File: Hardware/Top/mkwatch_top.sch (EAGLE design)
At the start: 64 parts, among them SW5 SWITCH.MOM, SW6 SWITCH.MOM, U1 NRF52832_MODULE_MDBT42, U4 FT231XS, U5 PCF8523

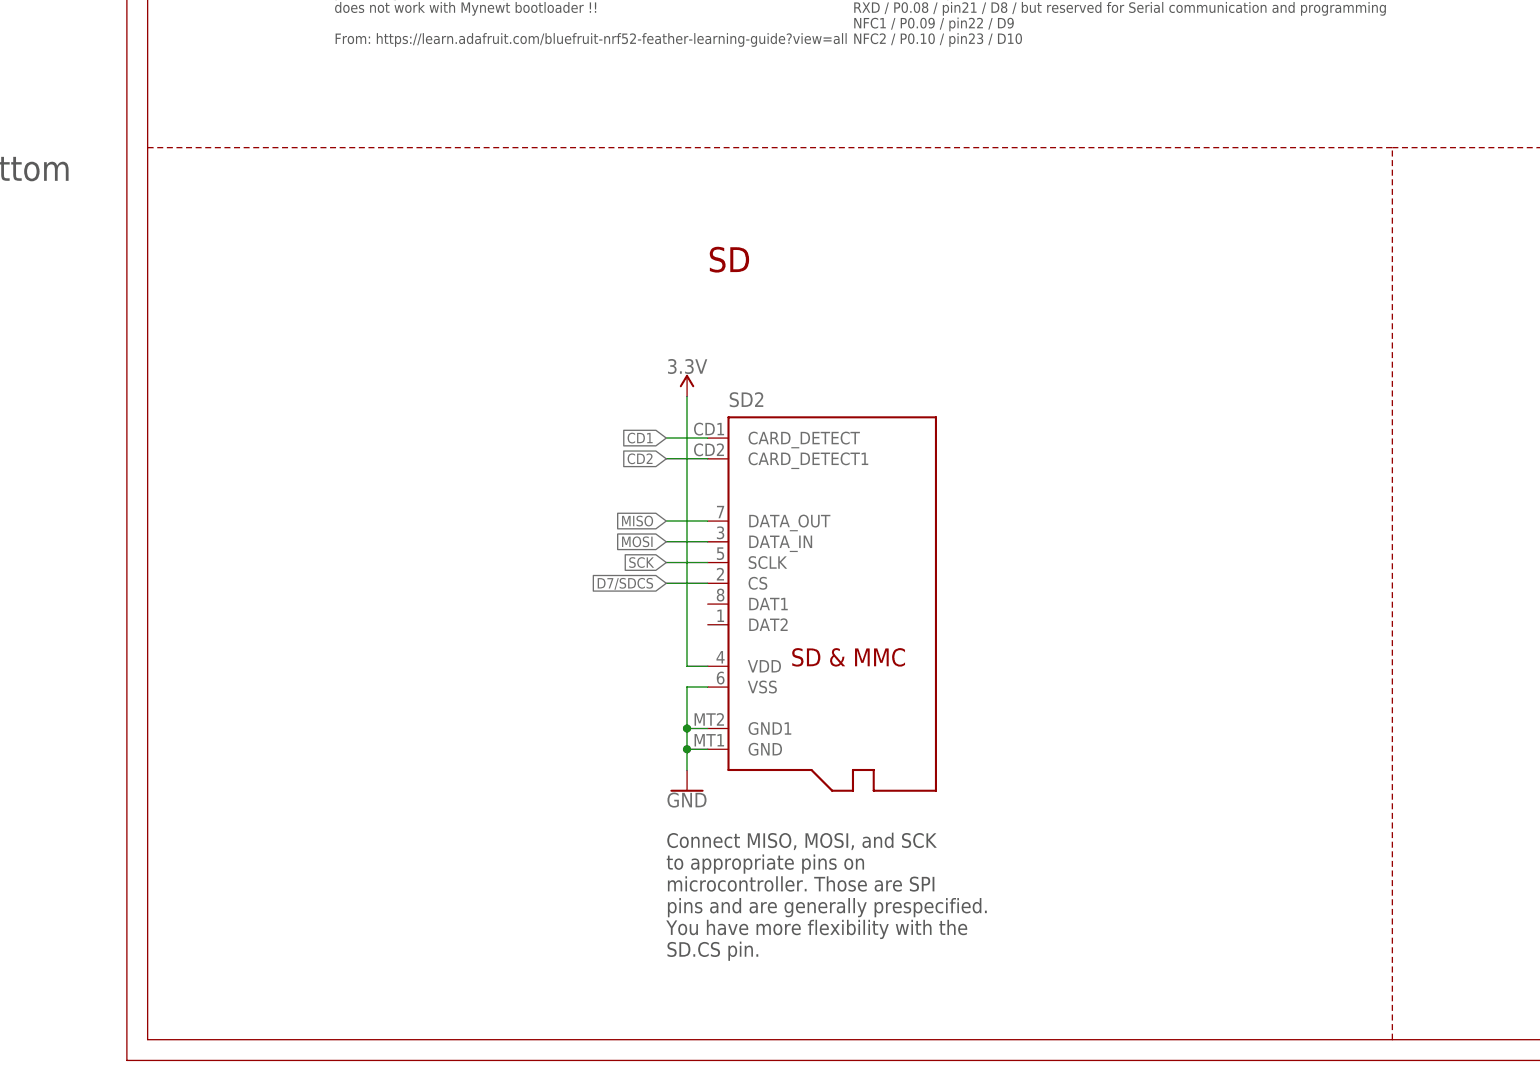
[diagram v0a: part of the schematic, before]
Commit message: added 7pin connector to schematic and board for comm between top and bottom board
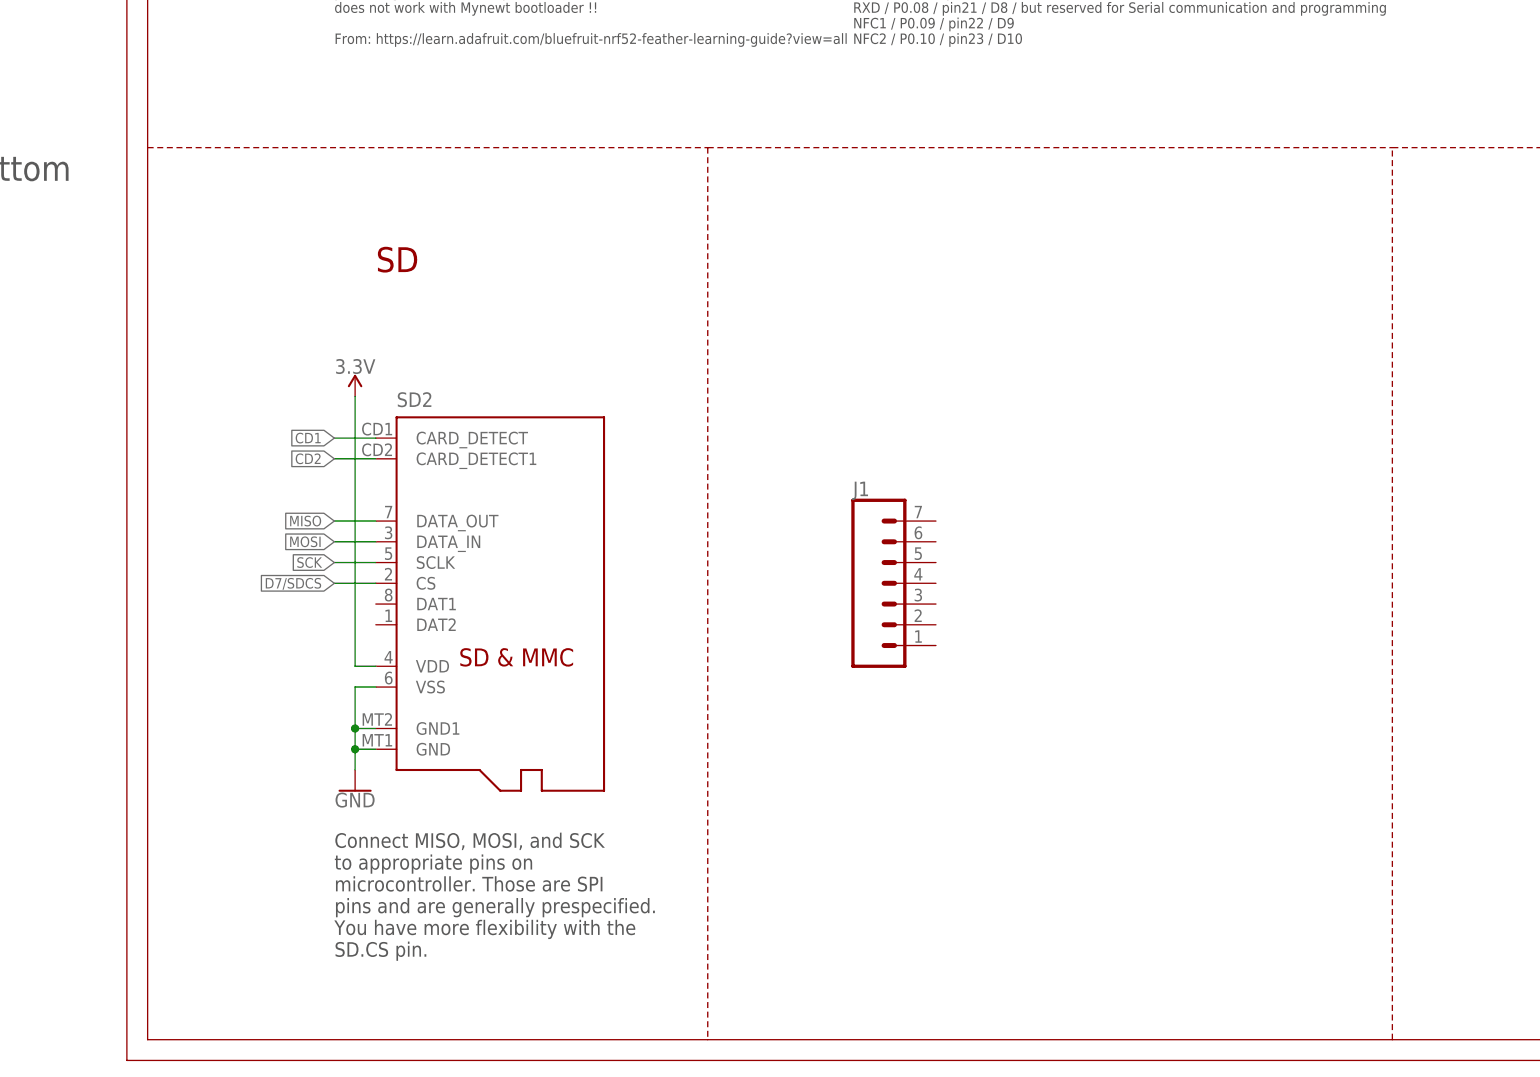
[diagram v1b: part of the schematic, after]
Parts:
- added J1: (no value), LinnesLab-Connectors:CONN_07-1.27MM
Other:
- moved on the sheet: SD2
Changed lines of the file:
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@@
 <part name="R9" library="LinnesLab-Passives" deviceset="RESISTOR" device="0402" package3d_urn="urn:adsk.eagle:package:15661898/2" value="10k"/>
 <part name="SUPPLY3" library="LinnesLab-Symbols" deviceset="3.3V" device=""/>
+<part name="J1" library="LinnesLab-Connectors" deviceset="CONN_07" device="-1.27MM"/>
 </parts>
 <sheets>
@@
 <text x="-83.82" y="-30.48" size="3.048" layer="94">Power Man.</text>
 <text x="73.66" y="-73.66" size="3.048" layer="94">Buttons</text>
-<text x="-238.76" y="-22.86" size="3.048" layer="94">SD</text>
+<text x="-279.4" y="-22.86" size="3.048" layer="94">SD</text>
 <text x="119.38" y="-48.26" size="1.27" layer="97">I2C Address = 0x68h</text>
 <text x="73.66" y="-50.8" size="1.27" layer="97">Back-up
@@
 <wire x1="-307.34" y1="162.56" x2="-307.34" y2="-7.62" width="0.1524" layer="94"/>
 <wire x1="-307.34" y1="-7.62" x2="-307.34" y2="-116.84" width="0.1524" layer="94"/>
-<wire x1="-307.34" y1="-116.84" x2="-154.94" y2="-116.84" width="0.1524" layer="94"/>
+<wire x1="-307.34" y1="-116.84" x2="-238.76" y2="-116.84" width="0.1524" layer="94"/>
+<wire x1="-238.76" y1="-116.84" x2="-154.94" y2="-116.84" width="0.1524" layer="94"/>
 <wire x1="-154.94" y1="-116.84" x2="15.24" y2="-116.84" width="0.1524" layer="94"/>
 <wire x1="15.24" y1="-116.84" x2="180.34" y2="-116.84" width="0.1524" layer="94"/>
@@
 <wire x1="53.34" y1="162.56" x2="-88.9" y2="162.56" width="0.1524" layer="94"/>
 <wire x1="-88.9" y1="162.56" x2="-307.34" y2="162.56" width="0.1524" layer="94"/>
-<wire x1="-307.34" y1="-7.62" x2="-154.94" y2="-7.62" width="0.1524" layer="94" style="dashdot"/>
+<wire x1="-307.34" y1="-7.62" x2="-238.76" y2="-7.62" width="0.1524" layer="94" style="dashdot"/>
+<wire x1="-238.76" y1="-7.62" x2="-154.94" y2="-7.62" width="0.1524" layer="94" style="dashdot"/>
 <wire x1="-154.94" y1="-116.84" x2="-154.94" y2="-7.62" width="0.1524" layer="94" style="dashdot"/>
 <wire x1="-154.94" y1="-7.62" x2="-88.9" y2="-7.62" width="0.1524" layer="94" style="dashdot"/>
@@
 <text x="-284.48" y="53.34" size="1.524" layer="97" font="vector" ratio="15">Additional notes for
 advanced users only</text>
-<text x="-243.84" y="-106.68" size="1.778" layer="97">Connect MISO, MOSI, and SCK
+<text x="-284.48" y="-106.68" size="1.778" layer="97">Connect MISO, MOSI, and SCK
 to appropriate pins on
 microcontroller. Those are SPI
@@
 way dynamically.</text>
 <text x="-27.94" y="88.9" size="1.778" layer="94">USB Bridge</text>
+<wire x1="-238.76" y1="-7.62" x2="-238.76" y2="-116.84" width="0.1524" layer="94" style="dashdot"/>
 </plain>
 <instances>
@@
 <attribute name="VALUE" x="-142.875" y="69.088" size="1.778" layer="96" font="vector" rot="R90" align="top-left"/>
 </instance>
-<instance part="SUPPLY5" gate="G$1" x="-241.3" y="-38.1" smashed="yes">
-<attribute name="VALUE" x="-241.3" y="-35.306" size="1.778" layer="96" align="bottom-center"/>
-</instance>
-<instance part="GND15" gate="G$1" x="-241.3" y="-86.36" smashed="yes">
-<attribute name="VALUE" x="-241.3" y="-86.614" size="1.778" layer="96" align="top-center"/>
-</instance>
-<instance part="SD2" gate="G$1" x="-220.98" y="-60.96" smashed="yes">
-<attribute name="NAME" x="-236.22" y="-39.37" size="1.778" layer="95"/>
-<attribute name="VALUE" x="-218.44" y="-39.37" size="1.778" layer="96"/>
+<instance part="SUPPLY5" gate="G$1" x="-281.94" y="-38.1" smashed="yes">
+<attribute name="VALUE" x="-281.94" y="-35.306" size="1.778" layer="96" align="bottom-center"/>
+</instance>
+<instance part="GND15" gate="G$1" x="-281.94" y="-86.36" smashed="yes">
+<attribute name="VALUE" x="-281.94" y="-86.614" size="1.778" layer="96" align="top-center"/>
+</instance>
+<instance part="SD2" gate="G$1" x="-261.62" y="-60.96" smashed="yes">
+<attribute name="NAME" x="-276.86" y="-39.37" size="1.778" layer="95"/>
+<attribute name="VALUE" x="-259.08" y="-39.37" size="1.778" layer="96"/>
 </instance>
 <instance part="R17" gate="G$1" x="-27.94" y="45.72" smashed="yes">
@@
 <instance part="SUPPLY3" gate="G$1" x="-287.02" y="149.86" smashed="yes">
 <attribute name="VALUE" x="-287.02" y="152.654" size="1.778" layer="96" align="bottom-center"/>
+</instance>
+<instance part="J1" gate="G$1" x="-215.9" y="-63.5" smashed="yes">
+<attribute name="VALUE" x="-220.98" y="-73.406" size="1.778" layer="96" font="vector"/>
+<attribute name="NAME" x="-220.98" y="-50.292" size="1.778" layer="95" font="vector"/>
 </instance>
 </instances>
@@
 </segment>
 <segment>
-<wire x1="-238.76" y1="-73.66" x2="-241.3" y2="-73.66" width="0.1524" layer="91"/>
+<wire x1="-279.4" y1="-73.66" x2="-281.94" y2="-73.66" width="0.1524" layer="91"/>
 <pinref part="GND15" gate="G$1" pin="GND"/>
-<wire x1="-241.3" y1="-73.66" x2="-241.3" y2="-78.74" width="0.1524" layer="91"/>
-<wire x1="-241.3" y1="-78.74" x2="-241.3" y2="-81.28" width="0.1524" layer="91"/>
-<wire x1="-241.3" y1="-81.28" x2="-241.3" y2="-83.82" width="0.1524" layer="91"/>
-<wire x1="-238.76" y1="-78.74" x2="-241.3" y2="-78.74" width="0.1524" layer="91"/>
-<junction x="-241.3" y="-78.74"/>
-<wire x1="-238.76" y1="-81.28" x2="-241.3" y2="-81.28" width="0.1524" layer="91"/>
-<junction x="-241.3" y="-81.28"/>
+<wire x1="-281.94" y1="-73.66" x2="-281.94" y2="-78.74" width="0.1524" layer="91"/>
+<wire x1="-281.94" y1="-78.74" x2="-281.94" y2="-81.28" width="0.1524" layer="91"/>
+<wire x1="-281.94" y1="-81.28" x2="-281.94" y2="-83.82" width="0.1524" layer="91"/>
+<wire x1="-279.4" y1="-78.74" x2="-281.94" y2="-78.74" width="0.1524" layer="91"/>
+<junction x="-281.94" y="-78.74"/>
+<wire x1="-279.4" y1="-81.28" x2="-281.94" y2="-81.28" width="0.1524" layer="91"/>
+<junction x="-281.94" y="-81.28"/>
 <pinref part="SD2" gate="G$1" pin="VSS"/>
 <pinref part="SD2" gate="G$1" pin="GND"/>
@@
 <segment>
 <pinref part="SUPPLY5" gate="G$1" pin="3.3V"/>
-<wire x1="-241.3" y1="-38.1" x2="-241.3" y2="-71.12" width="0.1524" layer="91"/>
-<wire x1="-241.3" y1="-71.12" x2="-238.76" y2="-71.12" width="0.1524" layer="91"/>
+<wire x1="-281.94" y1="-38.1" x2="-281.94" y2="-71.12" width="0.1524" layer="91"/>
+<wire x1="-281.94" y1="-71.12" x2="-279.4" y2="-71.12" width="0.1524" layer="91"/>
 <pinref part="SD2" gate="G$1" pin="VDD"/>
 </segment>
@@
 </segment>
 <segment>
-<wire x1="-243.84" y1="-58.42" x2="-238.76" y2="-58.42" width="0.1524" layer="91"/>
-<label x="-243.84" y="-58.42" size="1.27" layer="95" rot="R180" xref="yes"/>
+<wire x1="-284.48" y1="-58.42" x2="-279.4" y2="-58.42" width="0.1524" layer="91"/>
+<label x="-284.48" y="-58.42" size="1.27" layer="95" rot="R180" xref="yes"/>
 <pinref part="SD2" gate="G$1" pin="SCLK"/>
 </segment>
@@
 </segment>
 <segment>
-<wire x1="-243.84" y1="-55.88" x2="-238.76" y2="-55.88" width="0.1524" layer="91"/>
-<label x="-243.84" y="-55.88" size="1.27" layer="95" rot="R180" xref="yes"/>
+<wire x1="-284.48" y1="-55.88" x2="-279.4" y2="-55.88" width="0.1524" layer="91"/>
+<label x="-284.48" y="-55.88" size="1.27" layer="95" rot="R180" xref="yes"/>
 <pinref part="SD2" gate="G$1" pin="DATA_IN"/>
 </segment>
@@
 </segment>
 <segment>
-<wire x1="-243.84" y1="-53.34" x2="-238.76" y2="-53.34" width="0.1524" layer="91"/>
-<label x="-243.84" y="-53.34" size="1.27" layer="95" rot="R180" xref="yes"/>
+<wire x1="-284.48" y1="-53.34" x2="-279.4" y2="-53.34" width="0.1524" layer="91"/>
+<label x="-284.48" y="-53.34" size="1.27" layer="95" rot="R180" xref="yes"/>
 <pinref part="SD2" gate="G$1" pin="DATA_OUT"/>
 </segment>
@@
 <net name="CD2" class="0">
 <segment>
-<wire x1="-243.84" y1="-45.72" x2="-238.76" y2="-45.72" width="0.1524" layer="91"/>
-<label x="-243.84" y="-45.72" size="1.27" layer="95" rot="R180" xref="yes"/>
+<wire x1="-284.48" y1="-45.72" x2="-279.4" y2="-45.72" width="0.1524" layer="91"/>
+<label x="-284.48" y="-45.72" size="1.27" layer="95" rot="R180" xref="yes"/>
 <pinref part="SD2" gate="G$1" pin="CARD_DETECT1"/>
 </segment>
@@
 <net name="CD1" class="0">
 <segment>
-<wire x1="-243.84" y1="-43.18" x2="-238.76" y2="-43.18" width="0.1524" layer="91"/>
-<label x="-243.84" y="-43.18" size="1.27" layer="95" rot="R180" xref="yes"/>
+<wire x1="-284.48" y1="-43.18" x2="-279.4" y2="-43.18" width="0.1524" layer="91"/>
+<label x="-284.48" y="-43.18" size="1.27" layer="95" rot="R180" xref="yes"/>
 <pinref part="SD2" gate="G$1" pin="CARD_DETECT"/>
 </segment>
@@
 </segment>
 <segment>
-<wire x1="-243.84" y1="-60.96" x2="-238.76" y2="-60.96" width="0.1524" layer="91"/>
-<label x="-243.84" y="-60.96" size="1.27" layer="95" rot="R180" xref="yes"/>
+<wire x1="-284.48" y1="-60.96" x2="-279.4" y2="-60.96" width="0.1524" layer="91"/>
+<label x="-284.48" y="-60.96" size="1.27" layer="95" rot="R180" xref="yes"/>
 <pinref part="SD2" gate="G$1" pin="CS"/>
 </segment>

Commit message: WIP - positioned main components on top and bottom, starting to re arrange passives before routing begins
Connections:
- new net N$16: J1.7
- new net N$18: J1.6
- new net N$19: J1.5
- new net N$27: J1.3
- new net N$28: J1.2
- new net N$29: J1.1
- net 3.3V: now also R9.2
- net N$20: now also J1.4; no longer R9.2
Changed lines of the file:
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@@
 <part name="SUPPLY3" library="LinnesLab-Symbols" deviceset="3.3V" device=""/>
 <part name="J1" library="LinnesLab-Connectors" deviceset="CONN_07" device="-1.27MM"/>
+<part name="SUPPLY6" library="LinnesLab-Symbols" deviceset="3.3V" device=""/>
 </parts>
 <sheets>
@@
 <attribute name="NAME" x="-220.98" y="-50.292" size="1.778" layer="95" font="vector"/>
 </instance>
+<instance part="SUPPLY6" gate="G$1" x="-269.24" y="149.86" smashed="yes">
+<attribute name="VALUE" x="-269.24" y="152.654" size="1.778" layer="96" align="bottom-center"/>
+</instance>
 </instances>
 <busses>
@@
 <wire x1="-287.02" y1="147.32" x2="-287.02" y2="149.86" width="0.1524" layer="91"/>
 <pinref part="SUPPLY3" gate="G$1" pin="3.3V"/>
+</segment>
+<segment>
+<pinref part="R9" gate="G$1" pin="2"/>
+<wire x1="-269.24" y1="147.32" x2="-269.24" y2="149.86" width="0.1524" layer="91"/>
+<pinref part="SUPPLY6" gate="G$1" pin="3.3V"/>
 </segment>
 </net>
@@
 </segment>
 </net>
-<net name="N$20" class="0">
-<segment>
-<pinref part="R9" gate="G$1" pin="2"/>
-<wire x1="-269.24" y1="147.32" x2="-269.24" y2="149.86" width="0.1524" layer="91"/>
-</segment>
-</net>
 <net name="D27/CHGSTAT" class="0">
 <segment>
@@
 </segment>
 </net>
+<net name="N$16" class="0">
+<segment>
+<pinref part="J1" gate="G$1" pin="7"/>
+<wire x1="-210.82" y1="-53.34" x2="-205.74" y2="-53.34" width="0.1524" layer="91"/>
+</segment>
+</net>
+<net name="N$18" class="0">
+<segment>
+<pinref part="J1" gate="G$1" pin="6"/>
+<wire x1="-210.82" y1="-55.88" x2="-205.74" y2="-55.88" width="0.1524" layer="91"/>
+</segment>
+</net>
+<net name="N$19" class="0">
+<segment>
+<pinref part="J1" gate="G$1" pin="5"/>
+<wire x1="-210.82" y1="-58.42" x2="-205.74" y2="-58.42" width="0.1524" layer="91"/>
+</segment>
+</net>
+<net name="N$20" class="0">
+<segment>
+<pinref part="J1" gate="G$1" pin="4"/>
+<wire x1="-210.82" y1="-60.96" x2="-205.74" y2="-60.96" width="0.1524" layer="91"/>
+</segment>
+</net>
+<net name="N$27" class="0">
+<segment>
+<pinref part="J1" gate="G$1" pin="3"/>
+<wire x1="-210.82" y1="-63.5" x2="-205.74" y2="-63.5" width="0.1524" layer="91"/>
+</segment>
+</net>
+<net name="N$28" class="0">
+<segment>
+<pinref part="J1" gate="G$1" pin="2"/>
+<wire x1="-210.82" y1="-66.04" x2="-205.74" y2="-66.04" width="0.1524" layer="91"/>
+</segment>
+</net>
+<net name="N$29" class="0">
+<segment>
+<pinref part="J1" gate="G$1" pin="1"/>
+<wire x1="-210.82" y1="-68.58" x2="-205.74" y2="-68.58" width="0.1524" layer="91"/>
+</segment>
+</net>
